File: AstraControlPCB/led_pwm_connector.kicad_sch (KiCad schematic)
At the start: 12 parts, among them CN7 JST_VH_8PIN_10A_250V

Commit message: Silkscreen
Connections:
- net PWM_CH1 renamed GPIO_18_PWM_CH1
- net PWM_CH2 renamed GPIO_17_PWM_CH2
- net PWM_CH3 renamed GPIO_16_PWM_CH3
- net PWM_CH4 renamed GPIO_15_PWM_CH4
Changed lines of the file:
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@@
 		)
 	)
-	(hierarchical_label "PWM_CH3"
+	(hierarchical_label "GPIO_16_PWM_CH3"
 		(shape input)
 		(at 109.22 93.98 180)
@@
 		)
 	)
-	(hierarchical_label "PWM_CH2"
+	(hierarchical_label "GPIO_17_PWM_CH2"
 		(shape input)
 		(at 109.22 73.66 180)
@@
 		)
 	)
-	(hierarchical_label "PWM_CH4"
+	(hierarchical_label "GPIO_15_PWM_CH4"
 		(shape input)
 		(at 109.22 114.3 180)
@@
 		)
 	)
-	(hierarchical_label "PWM_CH1"
+	(hierarchical_label "GPIO_18_PWM_CH1"
 		(shape input)
 		(at 109.22 55.88 180)

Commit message: Added MFN MPR to each components for eurocircuits
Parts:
- CN7: MFN (none) -> JST; MPN (none) -> B8P-VH-B(LF)(SN)
- R36, R37, R38, R39, R40: MFN (none) -> UNI-ROYAL(Uniroyal Elec); MPN (none) -> 0805W8F0000T5E
- TP39, TP40, TP41, TP42, TP43: MFN (none) -> ronghe; MPN (none) -> RH-5000
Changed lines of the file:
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@@
 			)
 		)
-		(property "Description" ""
+		(property "Description" "1x8P 8P VH Tin 8 -25℃~+85℃ 10A 1 3.96mm Brass Direct Insert Plugin,P=3.96mm Wire To Board Connector ROHS"
 			(at 182.88 86.36 0)
 			(effects
@@
 					(bold yes)
 				)
+			)
+		)
+		(property "MFN" "JST"
+			(at 182.88 143.51 0)
+			(effects
+				(font
+					(size 1.27 1.27)
+				)
+				(hide yes)
+			)
+		)
+		(property "MPN" "B8P-VH-B(LF)(SN)"
+			(at 182.88 143.51 0)
+			(effects
+				(font
+					(size 1.27 1.27)
+				)
+				(hide yes)
 			)
 		)
@@
 			)
 		)
-		(property "Description" ""
+		(property "Description" "Test Points / Test Rings ROHS"
 			(at 124.46 48.26 90)
 			(effects
@@
 				)
 				(justify left)
+			)
+		)
+		(property "MFN" "ronghe"
+			(at 124.46 82.55 0)
+			(effects
+				(font
+					(size 1.27 1.27)
+				)
+				(hide yes)
+			)
+		)
+		(property "MPN" "RH-5000"
+			(at 124.46 82.55 0)
+			(effects
+				(font
+					(size 1.27 1.27)
+				)
+				(hide yes)
 			)
 		)
@@
 			)
 		)
-		(property "Description" "Thick Film Resistors"
+		(property "Description" "125mW Thick Film Resistors 150V ±800ppm/℃ ±1% 0Ω 0805 Chip Resistor - Surface Mount ROHS"
 			(at 116.84 40.64 0)
 			(effects
@@
 					(bold yes)
 				)
+			)
+		)
+		(property "MFN" "UNI-ROYAL(Uniroyal Elec)"
+			(at 116.84 55.88 0)
+			(effects
+				(font
+					(size 1.27 1.27)
+				)
+				(hide yes)
+			)
+		)
+		(property "MPN" "0805W8F0000T5E"
+			(at 116.84 55.88 0)
+			(effects
+				(font
+					(size 1.27 1.27)
+				)
+				(hide yes)
 			)
 		)
@@
 			)
 		)
-		(property "Description" "Thick Film Resistors"
+		(property "Description" "125mW Thick Film Resistors 150V ±800ppm/℃ ±1% 0Ω 0805 Chip Resistor - Surface Mount ROHS"
 			(at 116.84 78.74 0)
 			(effects
@@
 					(bold yes)
 				)
+			)
+		)
+		(property "MFN" "UNI-ROYAL(Uniroyal Elec)"
+			(at 116.84 93.98 0)
+			(effects
+				(font
+					(size 1.27 1.27)
+				)
+				(hide yes)
+			)
+		)
+		(property "MPN" "0805W8F0000T5E"
+			(at 116.84 93.98 0)
+			(effects
+				(font
+					(size 1.27 1.27)
+				)
+				(hide yes)
 			)
 		)
@@
 			)
 		)
-		(property "Description" ""
+		(property "Description" "Test Points / Test Rings ROHS"
 			(at 124.46 66.04 90)
 			(effects
@@
 				)
 				(justify left)
+			)
+		)
+		(property "MFN" "ronghe"
+			(at 124.46 100.33 0)
+			(effects
+				(font
+					(size 1.27 1.27)
+				)
+				(hide yes)
+			)
+		)
+		(property "MPN" "RH-5000"
+			(at 124.46 100.33 0)
+			(effects
+				(font
+					(size 1.27 1.27)
+				)
+				(hide yes)
 			)
 		)
@@
 			)
 		)
-		(property "Description" "Thick Film Resistors"
+		(property "Description" "125mW Thick Film Resistors 150V ±800ppm/℃ ±1% 0Ω 0805 Chip Resistor - Surface Mount ROHS"
 			(at 116.84 60.96 0)
 			(effects
@@
 					(bold yes)
 				)
+			)
+		)
+		(property "MFN" "UNI-ROYAL(Uniroyal Elec)"
+			(at 116.84 76.2 0)
+			(effects
+				(font
+					(size 1.27 1.27)
+				)
+				(hide yes)
+			)
+		)
+		(property "MPN" "0805W8F0000T5E"
+			(at 116.84 76.2 0)
+			(effects
+				(font
+					(size 1.27 1.27)
+				)
+				(hide yes)
 			)
 		)
@@
 			)
 		)
-		(property "Description" ""
+		(property "Description" "Test Points / Test Rings ROHS"
 			(at 124.46 106.68 90)
 			(effects
@@
 				)
 				(justify left)
+			)
+		)
+		(property "MFN" "ronghe"
+			(at 124.46 140.97 0)
+			(effects
+				(font
+					(size 1.27 1.27)
+				)
+				(hide yes)
+			)
+		)
+		(property "MPN" "RH-5000"
+			(at 124.46 140.97 0)
+			(effects
+				(font
+					(size 1.27 1.27)
+				)
+				(hide yes)
 			)
 		)
@@
 			)
 		)
-		(property "Description" ""
+		(property "Description" "Test Points / Test Rings ROHS"
 			(at 124.46 86.36 90)
 			(effects
@@
 				)
 				(justify left)
+			)
+		)
+		(property "MFN" "ronghe"
+			(at 124.46 120.65 0)
+			(effects
+				(font
+					(size 1.27 1.27)
+				)
+				(hide yes)
+			)
+		)
+		(property "MPN" "RH-5000"
+			(at 124.46 120.65 0)
+			(effects
+				(font
+					(size 1.27 1.27)
+				)
+				(hide yes)
 			)
 		)
@@
 			)
 		)
-		(property "Description" "Thick Film Resistors"
+		(property "Description" "125mW Thick Film Resistors 150V ±800ppm/℃ ±1% 0Ω 0805 Chip Resistor - Surface Mount ROHS"
 			(at 116.84 119.38 0)
 			(effects
@@
 					(bold yes)
 				)
+			)
+		)
+		(property "MFN" "UNI-ROYAL(Uniroyal Elec)"
+			(at 116.84 134.62 0)
+			(effects
+				(font
+					(size 1.27 1.27)
+				)
+				(hide yes)
+			)
+		)
+		(property "MPN" "0805W8F0000T5E"
+			(at 116.84 134.62 0)
+			(effects
+				(font
+					(size 1.27 1.27)
+				)
+				(hide yes)
 			)
 		)
@@
 			)
 		)
-		(property "Description" "Thick Film Resistors"
+		(property "Description" "125mW Thick Film Resistors 150V ±800ppm/℃ ±1% 0Ω 0805 Chip Resistor - Surface Mount ROHS"
 			(at 116.84 99.06 0)
 			(effects
@@
 					(bold yes)
 				)
+			)
+		)
+		(property "MFN" "UNI-ROYAL(Uniroyal Elec)"
+			(at 116.84 114.3 0)
+			(effects
+				(font
+					(size 1.27 1.27)
+				)
+				(hide yes)
+			)
+		)
+		(property "MPN" "0805W8F0000T5E"
+			(at 116.84 114.3 0)
+			(effects
+				(font
+					(size 1.27 1.27)
+				)
+				(hide yes)
 			)
 		)
@@
 			)
 		)
-		(property "Description" ""
+		(property "Description" "Test Points / Test Rings ROHS"
 			(at 124.46 27.94 90)
 			(effects
@@
 			)
 		)
+		(property "MFN" "ronghe"
+			(at 124.46 62.23 0)
+			(effects
+				(font
+					(size 1.27 1.27)
+				)
+				(hide yes)
+			)
+		)
+		(property "MPN" "RH-5000"
+			(at 124.46 62.23 0)
+			(effects
+				(font
+					(size 1.27 1.27)
+				)
+				(hide yes)
+			)
+		)

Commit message: Update schematic titles, templates
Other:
- title: AstraControl - Root -> AstraControl - PWM Connector
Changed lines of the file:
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@@
 	(paper "A4")
 	(title_block
-		(title "AstraControl - Root")
+		(title "AstraControl - PWM Connector")
 		(date "2024-08-26")
 		(rev "A")

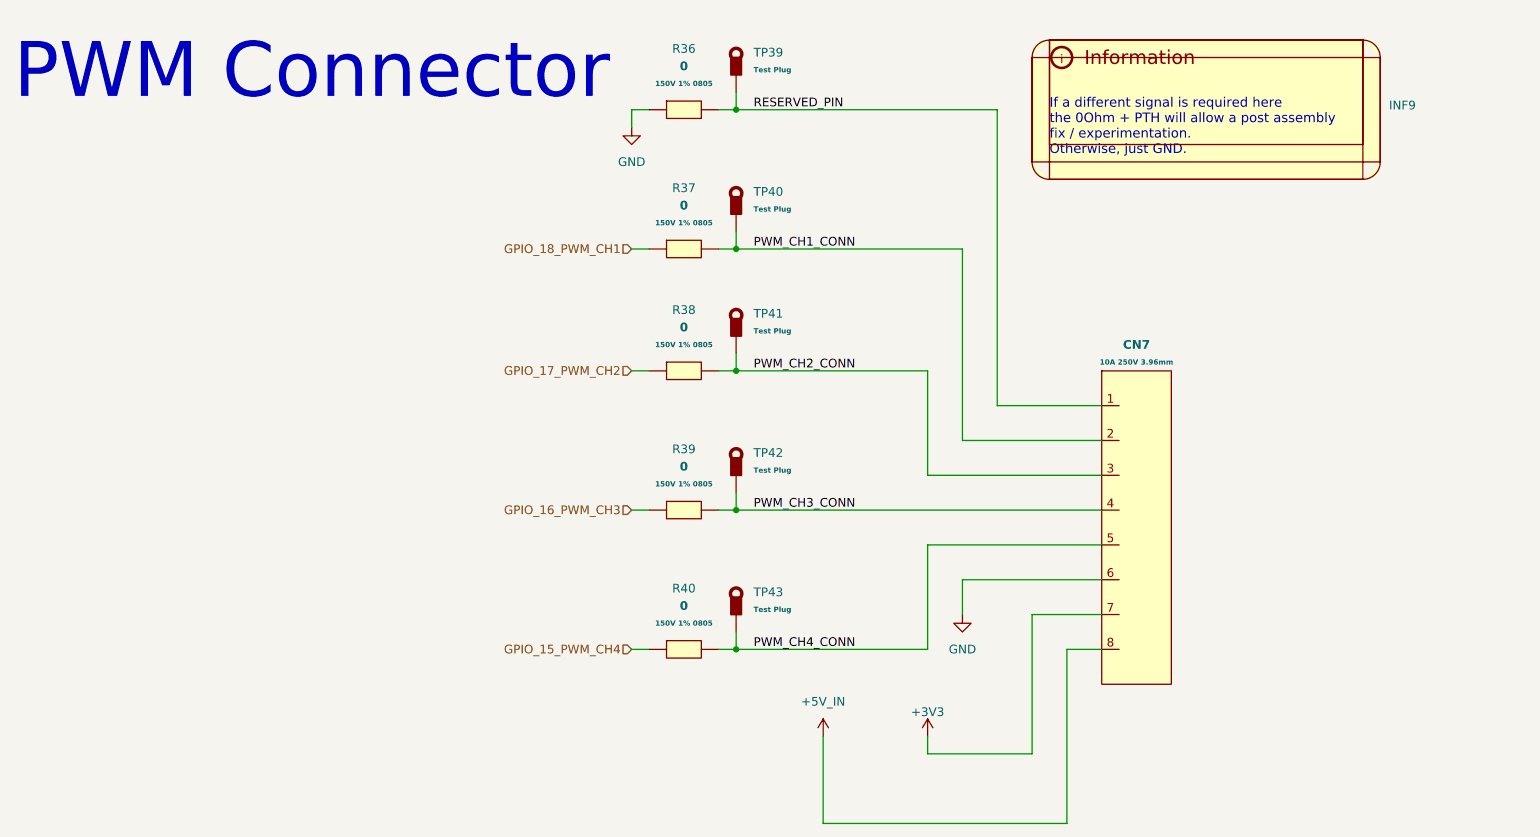
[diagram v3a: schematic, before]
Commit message: Update to new rs485 chip, use 2 bit 5v gpio
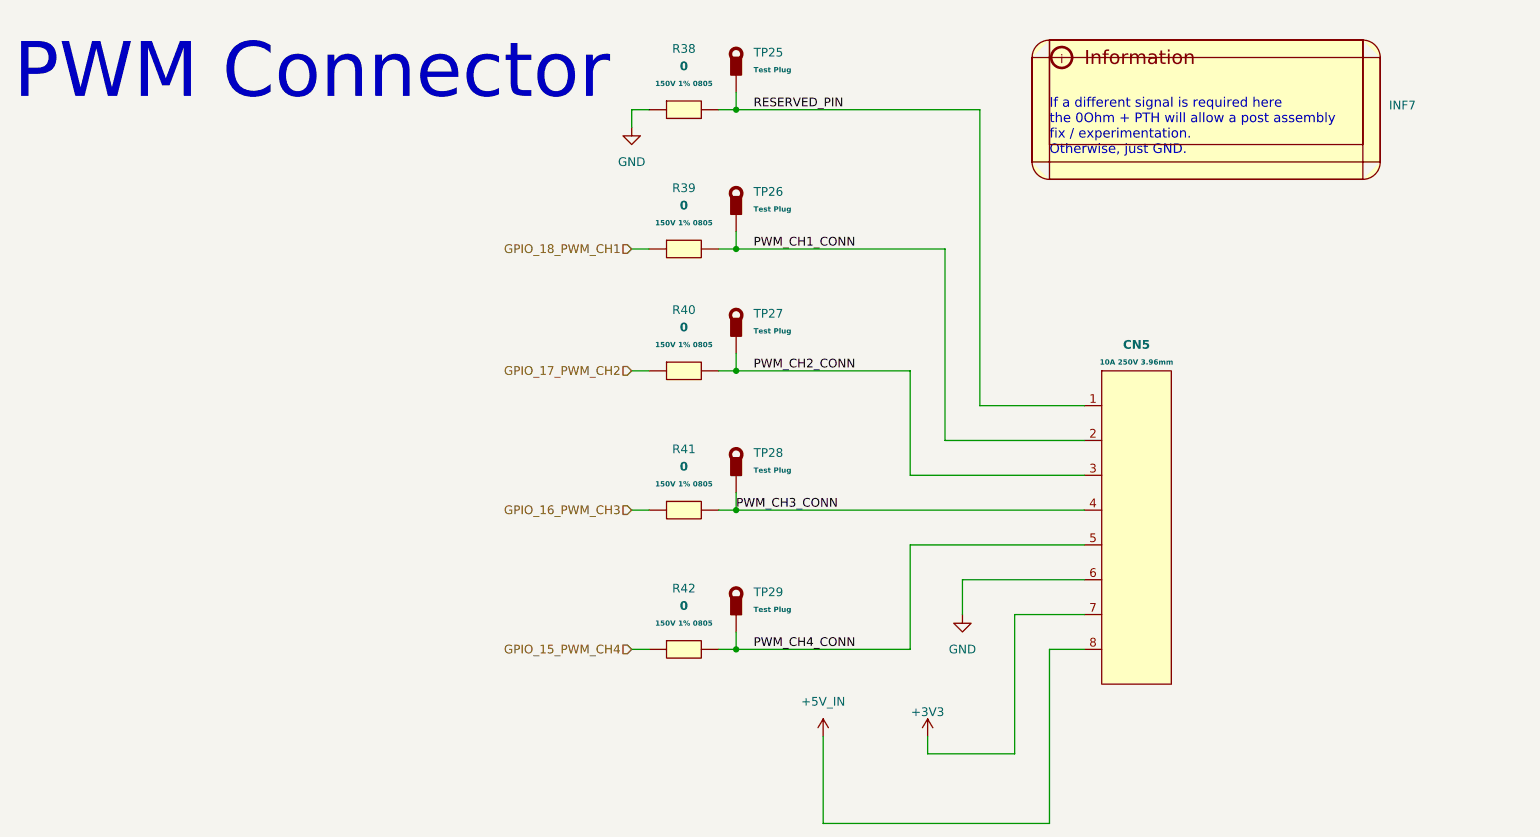
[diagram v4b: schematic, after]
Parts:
- renumbered CN7 to CN5, INF9 to INF7, R36 to R38, R37 to R39, R38 to R40, R39 to R41, R40 to R42, TP39 to TP25, TP40 to TP26, TP41 to TP27, TP42 to TP28, TP43 to TP29
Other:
- moved on the sheet: CN5
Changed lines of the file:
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@@
 	(wire
 		(pts
-			(xy 152.4 73.66) (xy 152.4 88.9)
+			(xy 149.86 73.66) (xy 149.86 88.9)
 		)
 		(stroke
@@
 	(wire
 		(pts
-			(xy 124.46 93.98) (xy 177.8 93.98)
-		)
-		(stroke
-			(width 0)
-			(type default)
-		)
-	)
-	(wire
-		(pts
-			(xy 152.4 99.06) (xy 152.4 114.3)
+			(xy 121.92 93.98) (xy 124.46 93.98)
+		)
+		(stroke
+			(width 0)
+			(type default)
+		)
+	)
+	(wire
+		(pts
+			(xy 149.86 99.06) (xy 149.86 114.3)
 		)
 		(stroke
@@
 	(wire
 		(pts
-			(xy 162.56 35.56) (xy 162.56 78.74)
+			(xy 160.02 35.56) (xy 160.02 78.74)
 		)
 		(stroke
@@
 	(wire
 		(pts
-			(xy 157.48 55.88) (xy 157.48 83.82)
+			(xy 154.94 55.88) (xy 154.94 83.82)
 		)
 		(stroke
@@
 	(wire
 		(pts
-			(xy 167.64 109.22) (xy 167.64 129.54)
+			(xy 165.1 109.22) (xy 165.1 129.54)
 		)
 		(stroke
@@
 	(wire
 		(pts
-			(xy 137.16 139.7) (xy 172.72 139.7)
+			(xy 137.16 139.7) (xy 170.18 139.7)
 		)
 		(stroke
@@
 	(wire
 		(pts
-			(xy 152.4 88.9) (xy 177.8 88.9)
+			(xy 149.86 88.9) (xy 175.26 88.9)
 		)
 		(stroke
@@
 	(wire
 		(pts
-			(xy 162.56 78.74) (xy 177.8 78.74)
+			(xy 160.02 78.74) (xy 175.26 78.74)
 		)
 		(stroke
@@
 	(wire
 		(pts
-			(xy 124.46 73.66) (xy 152.4 73.66)
+			(xy 124.46 73.66) (xy 149.86 73.66)
 		)
 		(stroke
@@
 	(wire
 		(pts
-			(xy 152.4 99.06) (xy 177.8 99.06)
-		)
-		(stroke
-			(width 0)
-			(type default)
-		)
-	)
-	(wire
-		(pts
-			(xy 172.72 114.3) (xy 177.8 114.3)
+			(xy 149.86 99.06) (xy 175.26 99.06)
+		)
+		(stroke
+			(width 0)
+			(type default)
+		)
+	)
+	(wire
+		(pts
+			(xy 170.18 114.3) (xy 175.26 114.3)
 		)
 		(stroke
@@
 	(wire
 		(pts
-			(xy 157.48 104.14) (xy 177.8 104.14)
-		)
-		(stroke
-			(width 0)
-			(type default)
-		)
-	)
-	(wire
-		(pts
-			(xy 124.46 114.3) (xy 152.4 114.3)
+			(xy 157.48 104.14) (xy 175.26 104.14)
+		)
+		(stroke
+			(width 0)
+			(type default)
+		)
+	)
+	(wire
+		(pts
+			(xy 124.46 114.3) (xy 149.86 114.3)
 		)
 		(stroke
@@
 	(wire
 		(pts
-			(xy 124.46 55.88) (xy 157.48 55.88)
-		)
-		(stroke
-			(width 0)
-			(type default)
-		)
-	)
-	(wire
-		(pts
-			(xy 172.72 114.3) (xy 172.72 139.7)
+			(xy 124.46 55.88) (xy 154.94 55.88)
+		)
+		(stroke
+			(width 0)
+			(type default)
+		)
+	)
+	(wire
+		(pts
+			(xy 170.18 114.3) (xy 170.18 139.7)
 		)
 		(stroke
@@
 	(wire
 		(pts
-			(xy 121.92 93.98) (xy 124.46 93.98)
-		)
-		(stroke
-			(width 0)
-			(type default)
-		)
-	)
-	(wire
-		(pts
-			(xy 157.48 83.82) (xy 177.8 83.82)
+			(xy 154.94 83.82) (xy 175.26 83.82)
 		)
 		(stroke
@@
 	(wire
 		(pts
-			(xy 152.4 129.54) (xy 167.64 129.54)
+			(xy 152.4 129.54) (xy 165.1 129.54)
 		)
 		(stroke
@@
 	(wire
 		(pts
-			(xy 124.46 35.56) (xy 162.56 35.56)
-		)
-		(stroke
-			(width 0)
-			(type default)
-		)
-	)
-	(wire
-		(pts
-			(xy 167.64 109.22) (xy 177.8 109.22)
+			(xy 124.46 35.56) (xy 160.02 35.56)
+		)
+		(stroke
+			(width 0)
+			(type default)
+		)
+	)
+	(wire
+		(pts
+			(xy 165.1 109.22) (xy 175.26 109.22)
 		)
 		(stroke
@@
 		(pts
 			(xy 121.92 35.56) (xy 124.46 35.56)
+		)
+		(stroke
+			(width 0)
+			(type default)
+		)
+	)
+	(wire
+		(pts
+			(xy 124.46 93.98) (xy 175.26 93.98)
 		)
 		(stroke
@@
 	)
 	(label "PWM_CH3_CONN"
-		(at 127 93.98 0)
+		(at 124.46 93.98 0)
 		(fields_autoplaced yes)
 		(effects
@@
 		(on_board yes)
 		(dnp no)
-		(property "Reference" "CN7"
+		(property "Reference" "CN5"
 			(at 182.88 69.85 0)
 			(effects
@@
 			(project "AstraControl"
 				(path "/9a751838-dce8-4d69-8a02-736625ac74e7/0db21d8e-3390-4d67-877f-0e5d98e37848/e7f4ae23-1ac9-4fa3-959c-a78f85f3f546"
-					(reference "CN7")
+					(reference "CN5")
 					(unit 1)
 				)
@@
 		(dnp no)
 		(fields_autoplaced yes)
-		(property "Reference" "TP40"
+		(property "Reference" "TP26"
 			(at 127 47.5276 0)
 			(effects
@@
 			(project "AstraControl"
 				(path "/9a751838-dce8-4d69-8a02-736625ac74e7/0db21d8e-3390-4d67-877f-0e5d98e37848/e7f4ae23-1ac9-4fa3-959c-a78f85f3f546"
-					(reference "TP40")
+					(reference "TP26")
 					(unit 1)
 				)
@@
 		(dnp no)
 		(fields_autoplaced yes)
-		(property "Reference" "#PWR080"
+		(property "Reference" "#PWR072"
 			(at 137.16 130.81 0)
 			(effects
@@
 			(project "AstraControl"
 				(path "/9a751838-dce8-4d69-8a02-736625ac74e7/0db21d8e-3390-4d67-877f-0e5d98e37848/e7f4ae23-1ac9-4fa3-959c-a78f85f3f546"
-					(reference "#PWR080")
+					(reference "#PWR072")
 					(unit 1)
 				)
@@
 		(on_board yes)
 		(dnp no)
-		(property "Reference" "#PWR081"
+		(property "Reference" "#PWR073"
 			(at 152.4 130.81 0)
 			(effects
@@
 			(project "AstraControl"
 				(path "/9a751838-dce8-4d69-8a02-736625ac74e7/0db21d8e-3390-4d67-877f-0e5d98e37848/e7f4ae23-1ac9-4fa3-959c-a78f85f3f546"
-					(reference "#PWR081")
+					(reference "#PWR073")
 					(unit 1)
 				)
@@
 		(dnp no)
 		(fields_autoplaced yes)
-		(property "Reference" "R36"
+		(property "Reference" "R38"
 			(at 116.84 26.67 0)
 			(effects
@@
 			(project "AstraControl"
 				(path "/9a751838-dce8-4d69-8a02-736625ac74e7/0db21d8e-3390-4d67-877f-0e5d98e37848/e7f4ae23-1ac9-4fa3-959c-a78f85f3f546"
-					(reference "R36")
+					(reference "R38")
 					(unit 1)
 				)
@@
 		(dnp no)
 		(fields_autoplaced yes)
-		(property "Reference" "#PWR082"
+		(property "Reference" "#PWR074"
 			(at 157.48 115.57 0)
 			(effects
@@
 			(project "AstraControl"
 				(path "/9a751838-dce8-4d69-8a02-736625ac74e7/0db21d8e-3390-4d67-877f-0e5d98e37848/e7f4ae23-1ac9-4fa3-959c-a78f85f3f546"
-					(reference "#PWR082")
+					(reference "#PWR074")
 					(unit 1)
 				)
@@
 		(dnp no)
 		(fields_autoplaced yes)
-		(property "Reference" "R38"
+		(property "Reference" "R40"
 			(at 116.84 64.77 0)
 			(effects
@@
 			(project "AstraControl"
 				(path "/9a751838-dce8-4d69-8a02-736625ac74e7/0db21d8e-3390-4d67-877f-0e5d98e37848/e7f4ae23-1ac9-4fa3-959c-a78f85f3f546"
-					(reference "R38")
+					(reference "R40")
 					(unit 1)
 				)
@@
 		(dnp no)
 		(fields_autoplaced yes)
-		(property "Reference" "TP41"
+		(property "Reference" "TP27"
 			(at 127 65.3076 0)
 			(effects
@@
 			(project "AstraControl"
 				(path "/9a751838-dce8-4d69-8a02-736625ac74e7/0db21d8e-3390-4d67-877f-0e5d98e37848/e7f4ae23-1ac9-4fa3-959c-a78f85f3f546"
-					(reference "TP41")
+					(reference "TP27")
 					(unit 1)
 				)
@@
 		(dnp no)
 		(fields_autoplaced yes)
-		(property "Reference" "R37"
+		(property "Reference" "R39"
 			(at 116.84 46.99 0)
 			(effects
@@
 			(project "AstraControl"
 				(path "/9a751838-dce8-4d69-8a02-736625ac74e7/0db21d8e-3390-4d67-877f-0e5d98e37848/e7f4ae23-1ac9-4fa3-959c-a78f85f3f546"
-					(reference "R37")
+					(reference "R39")
 					(unit 1)
 				)
@@
 		(dnp no)
 		(fields_autoplaced yes)
-		(property "Reference" "INF9"
+		(property "Reference" "INF7"
 			(at 219.71 34.9249 0)
 			(effects
@@
 			(project ""
 				(path "/9a751838-dce8-4d69-8a02-736625ac74e7/0db21d8e-3390-4d67-877f-0e5d98e37848/e7f4ae23-1ac9-4fa3-959c-a78f85f3f546"
-					(reference "INF9")
+					(reference "INF7")
 					(unit 1)
 				)
@@
 		(dnp no)
 		(fields_autoplaced yes)
-		(property "Reference" "#PWR079"
+		(property "Reference" "#PWR071"
 			(at 109.22 44.45 0)
 			(effects
@@
 			(project "AstraControl"
 				(path "/9a751838-dce8-4d69-8a02-736625ac74e7/0db21d8e-3390-4d67-877f-0e5d98e37848/e7f4ae23-1ac9-4fa3-959c-a78f85f3f546"
-					(reference "#PWR079")
+					(reference "#PWR071")
 					(unit 1)
 				)
@@
 		(dnp no)
 		(fields_autoplaced yes)
-		(property "Reference" "TP43"
+		(property "Reference" "TP29"
 			(at 127 105.9476 0)
 			(effects
@@
 			(project "AstraControl"
 				(path "/9a751838-dce8-4d69-8a02-736625ac74e7/0db21d8e-3390-4d67-877f-0e5d98e37848/e7f4ae23-1ac9-4fa3-959c-a78f85f3f546"
-					(reference "TP43")
+					(reference "TP29")
 					(unit 1)
 				)
@@
 		(dnp no)
 		(fields_autoplaced yes)
-		(property "Reference" "TP42"
+		(property "Reference" "TP28"
 			(at 127 85.6276 0)
 			(effects
@@
 			(project "AstraControl"
 				(path "/9a751838-dce8-4d69-8a02-736625ac74e7/0db21d8e-3390-4d67-877f-0e5d98e37848/e7f4ae23-1ac9-4fa3-959c-a78f85f3f546"
-					(reference "TP42")
+					(reference "TP28")
 					(unit 1)
 				)
@@
 		(dnp no)
 		(fields_autoplaced yes)
-		(property "Reference" "R40"
+		(property "Reference" "R42"
 			(at 116.84 105.41 0)
 			(effects
@@
 			(project "AstraControl"
 				(path "/9a751838-dce8-4d69-8a02-736625ac74e7/0db21d8e-3390-4d67-877f-0e5d98e37848/e7f4ae23-1ac9-4fa3-959c-a78f85f3f546"
-					(reference "R40")
+					(reference "R42")
 					(unit 1)
 				)
@@
 		(dnp no)
 		(fields_autoplaced yes)
-		(property "Reference" "R39"
+		(property "Reference" "R41"
 			(at 116.84 85.09 0)
 			(effects
@@
 			(project "AstraControl"
 				(path "/9a751838-dce8-4d69-8a02-736625ac74e7/0db21d8e-3390-4d67-877f-0e5d98e37848/e7f4ae23-1ac9-4fa3-959c-a78f85f3f546"
-					(reference "R39")
+					(reference "R41")
 					(unit 1)
 				)
@@
 		(dnp no)
 		(fields_autoplaced yes)
-		(property "Reference" "TP39"
+		(property "Reference" "TP25"
 			(at 127 27.2076 0)
 			(effects
@@
 			(project "AstraControl"
 				(path "/9a751838-dce8-4d69-8a02-736625ac74e7/0db21d8e-3390-4d67-877f-0e5d98e37848/e7f4ae23-1ac9-4fa3-959c-a78f85f3f546"
-					(reference "TP39")
+					(reference "TP25")
 					(unit 1)
 				)
